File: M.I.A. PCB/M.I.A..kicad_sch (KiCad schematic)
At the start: 41 parts, among them J1 USB_C_Receptacle_USB2.0_16P, SW1 SW_Push, SW2 SW_Push, U1 W25Q128JVS, U2 RP2350B-QFN80, Y1 ABM8-272-T3

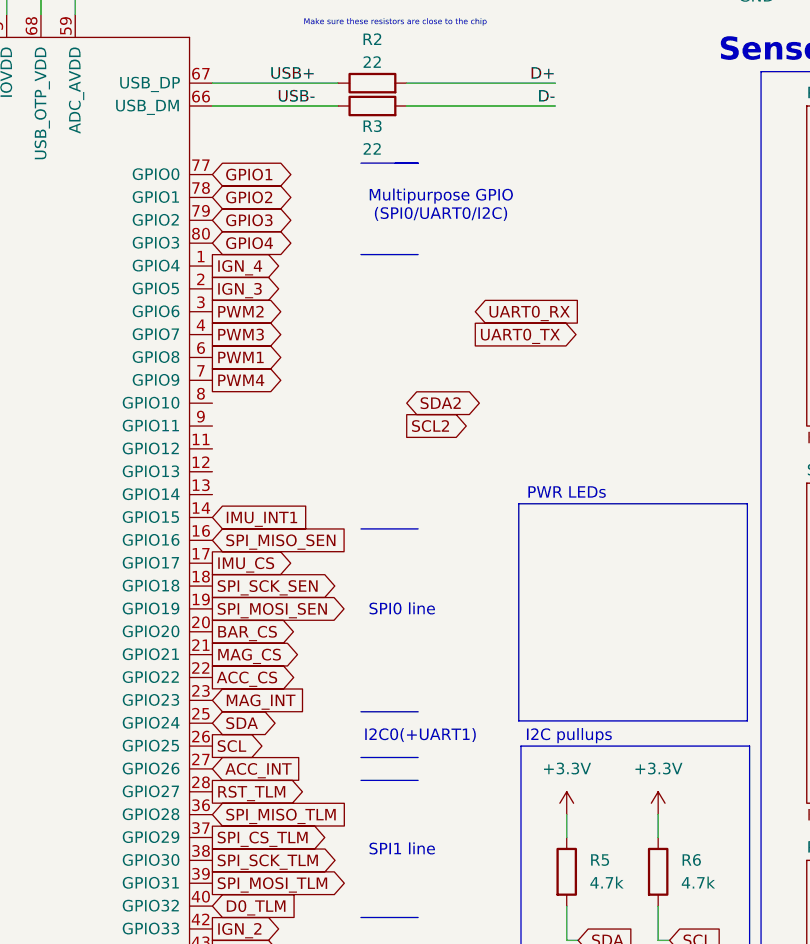
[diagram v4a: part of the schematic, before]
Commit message: Routed GPS Maybe Correctly
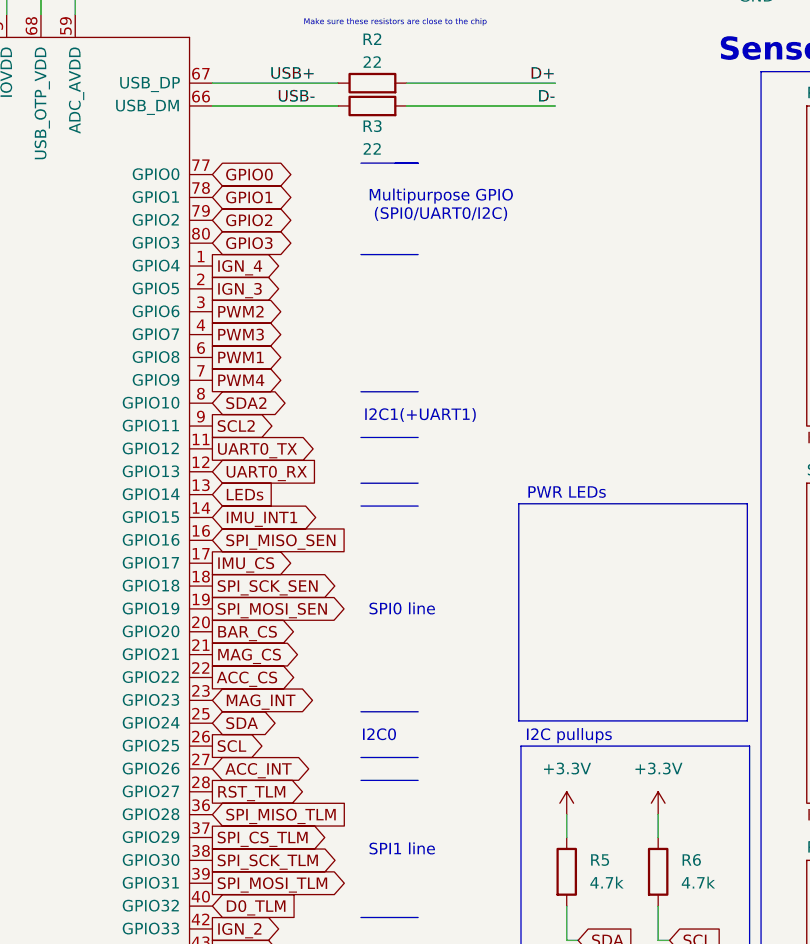
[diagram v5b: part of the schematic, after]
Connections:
- net GPIO4 is gone; now on net GPIO3: U2.80 (GPIO3)
- net GPIO1: now also U2.78 (GPIO1); no longer U2.77 (GPIO0)
- net GPIO2: now also U2.79 (GPIO2); no longer U2.78 (GPIO1)
- net GPIO3: no longer U2.79 (GPIO2)
- net SCL2: now also U2.9 (GPIO11)
- net SDA2: now also U2.8 (GPIO10)
- net UART0_RX: now also U2.12 (GPIO13)
- net UART0_TX: now also U2.11 (GPIO12)
- net LEDs: now reaches U2.13 (GPIO14)
- new net GPIO0: U2.77 (GPIO0)
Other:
- note added: "I2C0"
- note added: "I2C1(+UART1)"
- note removed: "I2C0(+UART1)"
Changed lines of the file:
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@@
 		)
 	)
-	(text "I2C0(+UART1)"
+	(text "I2C0"
 		(exclude_from_sim no)
-		(at 189.484 112.014 0)
+		(at 184.912 112.014 0)
+		(effects
+			(font
+				(size 1.27 1.27)
+			)
+		)
+	)
+	(text "I2C1(+UART1)"
+		(exclude_from_sim no)
+		(at 189.484 76.454 0)
 		(effects
 			(font
@@
 		)
 	)
+	(polyline
+		(pts
+			(xy 182.88 83.82) (xy 189.23 83.82)
+		)
+		(stroke
+			(width 0)
+			(type default)
+		)
+	)
 	(wire
 		(pts
@@
 		)
 	)
+	(polyline
+		(pts
+			(xy 182.88 78.74) (xy 189.23 78.74)
+		)
+		(stroke
+			(width 0)
+			(type default)
+		)
+	)
 	(wire
 		(pts
@@
 	(polyline
 		(pts
-			(xy 182.88 88.9) (xy 189.23 88.9)
+			(xy 182.88 86.36) (xy 189.23 86.36)
 		)
 		(stroke
@@
 		)
 	)
+	(polyline
+		(pts
+			(xy 182.88 73.66) (xy 189.23 73.66)
+		)
+		(stroke
+			(width 0)
+			(type default)
+		)
+	)
 	(wire
 		(pts
@@
 	)
 	(global_label "MAG_INT"
-		(shape input)
+		(shape bidirectional)
 		(at 166.37 107.95 0)
 		(fields_autoplaced yes)
@@
 		)
 		(property "Intersheetrefs" "${INTERSHEET_REFS}"
-			(at 176.8543 107.95 0)
+			(at 178.147 107.95 0)
 			(effects
 				(font
@@
 	(global_label "UART0_TX"
 		(shape output)
-		(at 195.58 67.31 0)
+		(at 166.37 80.01 0)
 		(fields_autoplaced yes)
 		(effects
@@
 		)
 		(property "Intersheetrefs" "${INTERSHEET_REFS}"
-			(at 207.5761 67.31 0)
+			(at 178.3661 80.01 0)
 			(effects
 				(font
@@
 		)
 	)
+	(global_label "GPIO0"
+		(shape bidirectional)
+		(at 166.37 49.53 0)
+		(fields_autoplaced yes)
+		(effects
+			(font
+				(size 1.27 1.27)
+			)
+			(justify left)
+		)
+		(property "Intersheetrefs" "${INTERSHEET_REFS}"
+			(at 176.1513 49.53 0)
+			(effects
+				(font
+					(size 1.27 1.27)
+				)
+				(justify left)
+				(hide yes)
+			)
+		)
+	)
 	(global_label "PWM4"
 		(shape output)
@@
 	(global_label "GPIO1"
 		(shape bidirectional)
-		(at 166.37 49.53 0)
+		(at 166.37 52.07 0)
 		(fields_autoplaced yes)
 		(effects
@@
 		)
 		(property "Intersheetrefs" "${INTERSHEET_REFS}"
-			(at 176.1513 49.53 0)
+			(at 176.1513 52.07 0)
 			(effects
 				(font
@@
 	(global_label "UART0_RX"
 		(shape input)
-		(at 195.58 64.77 0)
+		(at 166.37 82.55 0)
 		(fields_autoplaced yes)
 		(effects
@@
 		)
 		(property "Intersheetrefs" "${INTERSHEET_REFS}"
-			(at 207.8785 64.77 0)
+			(at 178.6685 82.55 0)
 			(effects
 				(font
@@
 	(global_label "GPIO3"
 		(shape bidirectional)
-		(at 166.37 54.61 0)
+		(at 166.37 57.15 0)
 		(fields_autoplaced yes)
 		(effects
@@
 		)
 		(property "Intersheetrefs" "${INTERSHEET_REFS}"
-			(at 176.1513 54.61 0)
+			(at 176.1513 57.15 0)
 			(effects
 				(font
@@
 	(global_label "SDA2"
 		(shape bidirectional)
-		(at 187.96 74.93 0)
+		(at 166.37 74.93 0)
 		(fields_autoplaced yes)
 		(effects
@@
 		)
 		(property "Intersheetrefs" "${INTERSHEET_REFS}"
-			(at 196.8341 74.93 0)
+			(at 175.2441 74.93 0)
 			(effects
 				(font
@@
 	)
 	(global_label "IMU_INT1"
-		(shape input)
+		(shape bidirectional)
 		(at 166.37 87.63 0)
 		(fields_autoplaced yes)
@@
 		)
 		(property "Intersheetrefs" "${INTERSHEET_REFS}"
-			(at 177.8219 87.63 0)
+			(at 178.9332 87.63 0)
 			(effects
 				(font
@@
 		)
 	)
+	(global_label "LEDs"
+		(shape input)
+		(at 166.37 85.09 0)
+		(fields_autoplaced yes)
+		(effects
+			(font
+				(size 1.27 1.27)
+			)
+			(justify left)
+		)
+		(property "Intersheetrefs" "${INTERSHEET_REFS}"
+			(at 173.8304 85.09 0)
+			(effects
+				(font
+					(size 1.27 1.27)
+				)
+				(justify left)
+				(hide yes)
+			)
+		)
+	)
 	(global_label "Cont_Sense2"
 		(shape output)
@@
 	(global_label "GPIO2"
 		(shape bidirectional)
-		(at 166.37 52.07 0)
+		(at 166.37 54.61 0)
 		(fields_autoplaced yes)
 		(effects
@@
 		)
 		(property "Intersheetrefs" "${INTERSHEET_REFS}"
-			(at 176.1513 52.07 0)
+			(at 176.1513 54.61 0)
 			(effects
 				(font
@@
 		)
 	)
-	(global_label "GPIO4"
-		(shape bidirectional)
-		(at 166.37 57.15 0)
-		(fields_autoplaced yes)
-		(effects
-			(font
-				(size 1.27 1.27)
-			)
-			(justify left)
-		)
-		(property "Intersheetrefs" "${INTERSHEET_REFS}"
-			(at 176.1513 57.15 0)
-			(effects
-				(font
-					(size 1.27 1.27)
-				)
-				(justify left)
-				(hide yes)
-			)
-		)
-	)
 	(global_label "SPI_SCK_SD"
 		(shape output)
@@
 	)
 	(global_label "ACC_INT"
-		(shape input)
+		(shape bidirectional)
 		(at 166.37 115.57 0)
 		(fields_autoplaced yes)
@@
 		)
 		(property "Intersheetrefs" "${INTERSHEET_REFS}"
-			(at 177.0357 115.57 0)
+			(at 177.9656 115.57 0)
 			(effects
 				(font
@@
 	(global_label "SCL2"
 		(shape output)
-		(at 187.96 77.47 0)
+		(at 166.37 77.47 0)
 		(fields_autoplaced yes)
 		(effects
@@
 		)
 		(property "Intersheetrefs" "${INTERSHEET_REFS}"
-			(at 195.6623 77.47 0)
+			(at 174.0723 77.47 0)
 			(effects
 				(font

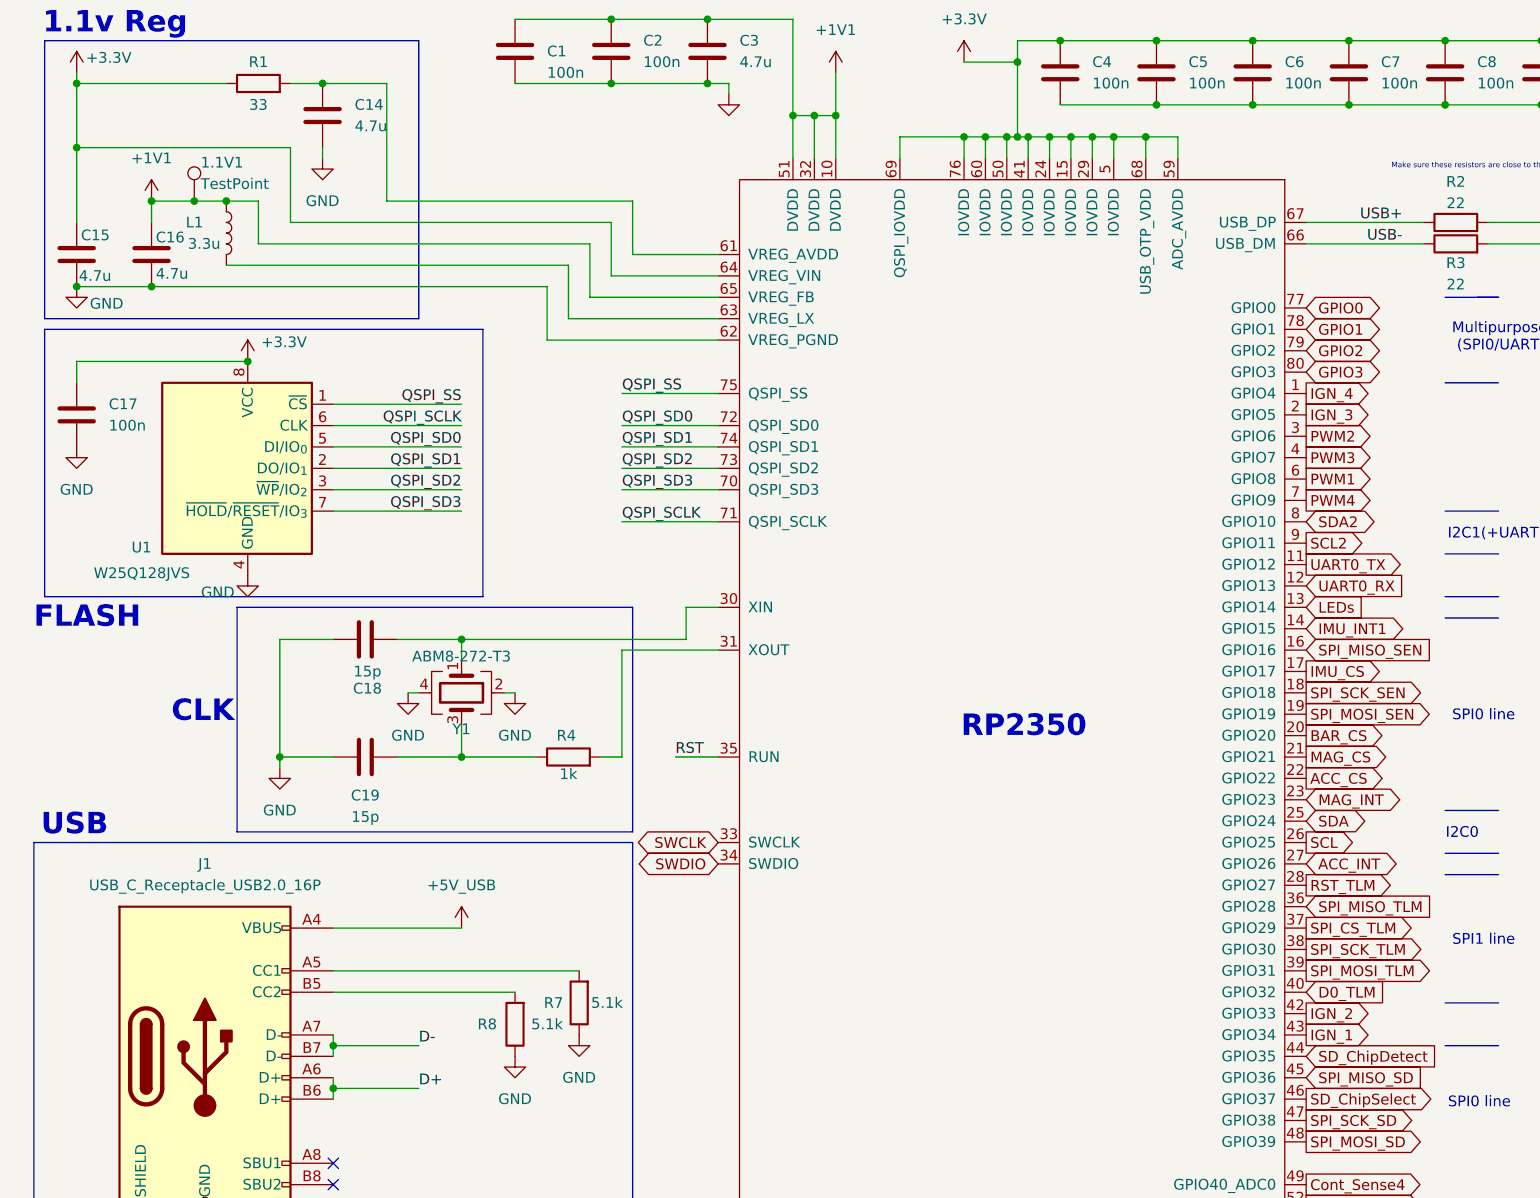
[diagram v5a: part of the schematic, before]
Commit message: Routed two ignition lines
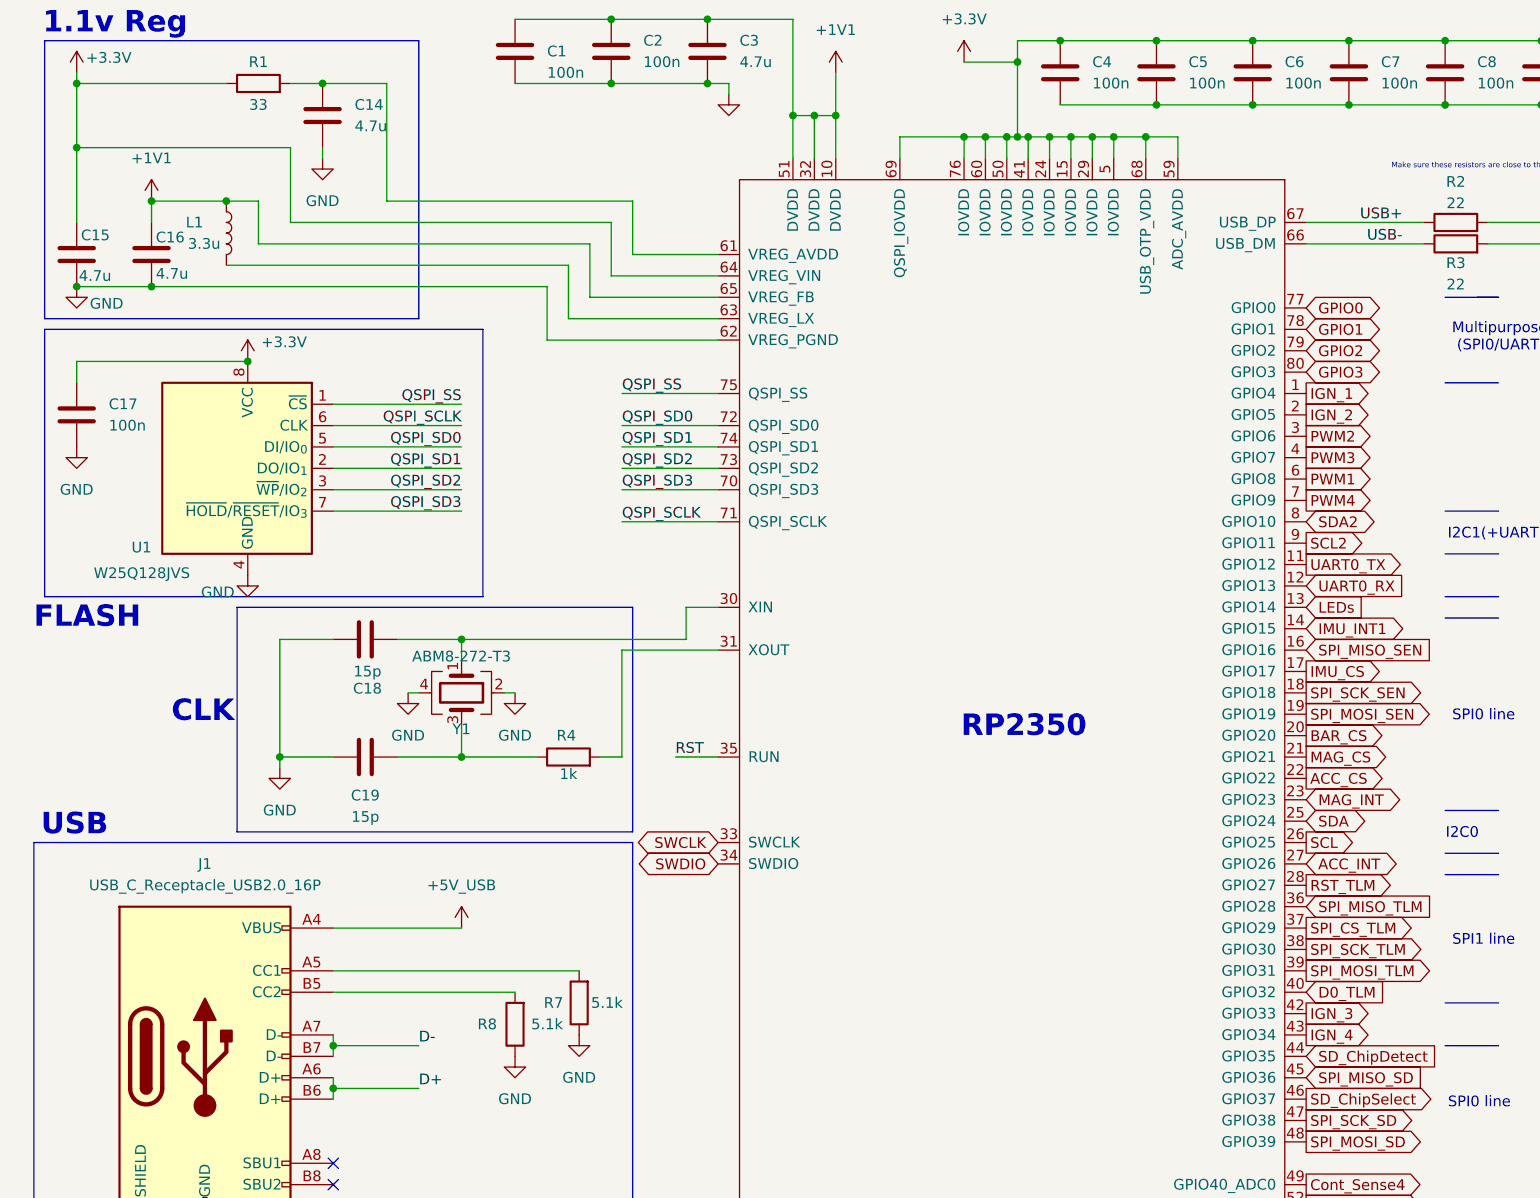
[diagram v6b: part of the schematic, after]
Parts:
- removed 1.1V1: TestPoint, TestPoint:TestPoint_Pad_D1.0mm, symbol Connector:TestPoint
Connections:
- net IGN_1: now also U2.1 (GPIO4); no longer U2.43 (GPIO34)
- net IGN_2: now also U2.2 (GPIO5); no longer U2.42 (GPIO33)
- net IGN_3: now also U2.42 (GPIO33); no longer U2.2 (GPIO5)
- net IGN_4: now also U2.43 (GPIO34); no longer U2.1 (GPIO4)
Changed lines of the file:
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@@
 	)
 	(junction
-		(at 34.29 36.83)
-		(diameter 0)
-		(color 0 0 0 0)
-	)
-	(junction
 		(at 83.82 22.86)
 		(diameter 0)
@@
 	(wire
 		(pts
-			(xy 34.29 36.83) (xy 29.21 36.83)
+			(xy 29.21 36.83) (xy 38.1 36.83)
 		)
 		(stroke
@@
 	(wire
 		(pts
-			(xy 38.1 36.83) (xy 34.29 36.83)
-		)
-		(stroke
-			(width 0)
-			(type default)
-		)
-	)
-	(wire
-		(pts
 			(xy 60.96 181.61) (xy 63.5 181.61)
 		)
@@
 	(global_label "IGN_3"
 		(shape output)
-		(at 166.37 62.23 0)
+		(at 166.37 133.35 0)
 		(fields_autoplaced yes)
 		(effects
@@
 		)
 		(property "Intersheetrefs" "${INTERSHEET_REFS}"
-			(at 174.7376 62.23 0)
+			(at 174.7376 133.35 0)
 			(effects
 				(font
@@
 	(global_label "IGN_2"
 		(shape output)
-		(at 166.37 133.35 0)
+		(at 166.37 62.23 0)
 		(fields_autoplaced yes)
 		(effects
@@
 		)
 		(property "Intersheetrefs" "${INTERSHEET_REFS}"
-			(at 174.7376 133.35 0)
+			(at 174.7376 62.23 0)
 			(effects
 				(font
@@
 	(global_label "IGN_1"
 		(shape output)
-		(at 166.37 135.89 0)
+		(at 166.37 59.69 0)
 		(fields_autoplaced yes)
 		(effects
@@
 		)
 		(property "Intersheetrefs" "${INTERSHEET_REFS}"
-			(at 174.7376 135.89 0)
+			(at 174.7376 59.69 0)
 			(effects
 				(font
@@
 	(global_label "IGN_4"
 		(shape output)
-		(at 166.37 59.69 0)
+		(at 166.37 135.89 0)
 		(fields_autoplaced yes)
 		(effects
@@
 		)
 		(property "Intersheetrefs" "${INTERSHEET_REFS}"
-			(at 174.7376 59.69 0)
+			(at 174.7376 135.89 0)
 			(effects
 				(font
@@
 					(unit 1)
 				)
-			)
-		)
-	)
-	(symbol
-		(lib_id "Connector:TestPoint")
-		(at 34.29 36.83 0)
-		(unit 1)
-		(exclude_from_sim no)
-		(in_bom yes)
-		(on_board yes)
-		(dnp no)
-		(property "Reference" "1.1V1"
-			(at 35.052 32.258 0)
-			(effects
-				(font
-					(size 1.27 1.27)
-				)
-				(justify left)
-			)
-		)
-		(property "Value" "TestPoint"
-			(at 35.052 34.798 0)
-			(effects
-				(font
-					(size 1.27 1.27)
-				)
-				(justify left)
-			)
-		)
-		(property "Footprint" "TestPoint:TestPoint_Pad_D1.0mm"
-			(at 39.37 36.83 0)
-			(effects
-				(font
-					(size 1.27 1.27)
-				)
-				(hide yes)
-			)
-		)
-		(property "Datasheet" "~"
-			(at 39.37 36.83 0)
-			(effects
-				(font
-					(size 1.27 1.27)
-				)
-				(hide yes)
-			)
-		)
-		(property "Description" "test point"
-			(at 34.29 36.83 0)
-			(effects
-				(font
-					(size 1.27 1.27)
-				)
-				(hide yes)
-			)
-		)
-		(property "LCSC" ""
-			(at 34.29 36.83 0)
-			(effects
-				(font
-					(size 1.27 1.27)
-				)
-				(hide yes)
-			)
-		)
-		(property "Manufacturer" ""
-			(at 34.29 36.83 0)
-			(effects
-				(font
-					(size 1.27 1.27)
-				)
-				(hide yes)
-			)
-		)
-		(property "Manufacturer Part" ""
-			(at 34.29 36.83 0)
-			(effects
-				(font
-					(size 1.27 1.27)
-				)
-				(hide yes)
-			)
-		)
-		(pin "1"
-		)
-		(instances
-			(project "M.I.A."
-				(path "/4d55825e-4251-44bf-9376-9abd9228f348"
-					(reference "1.1V1")
-					(unit 1)
-				)

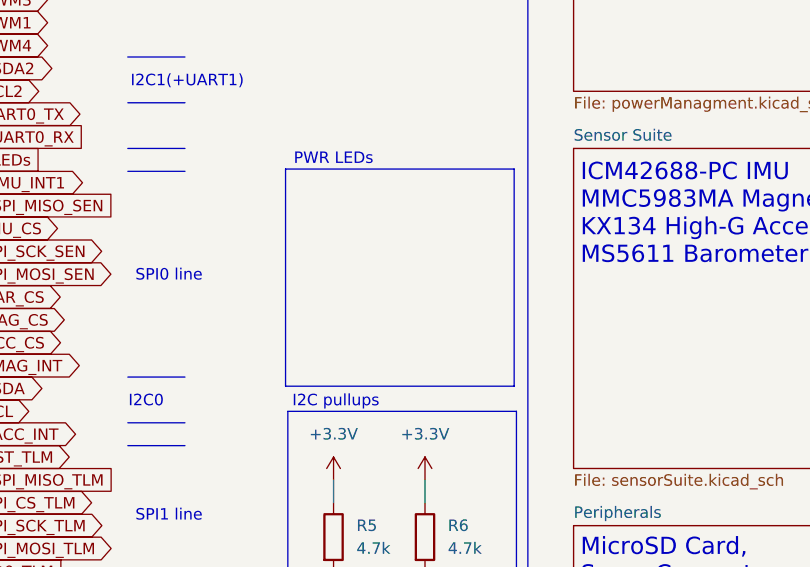
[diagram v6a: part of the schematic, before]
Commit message: Added LEDs, Prepped for 4 layer conversion
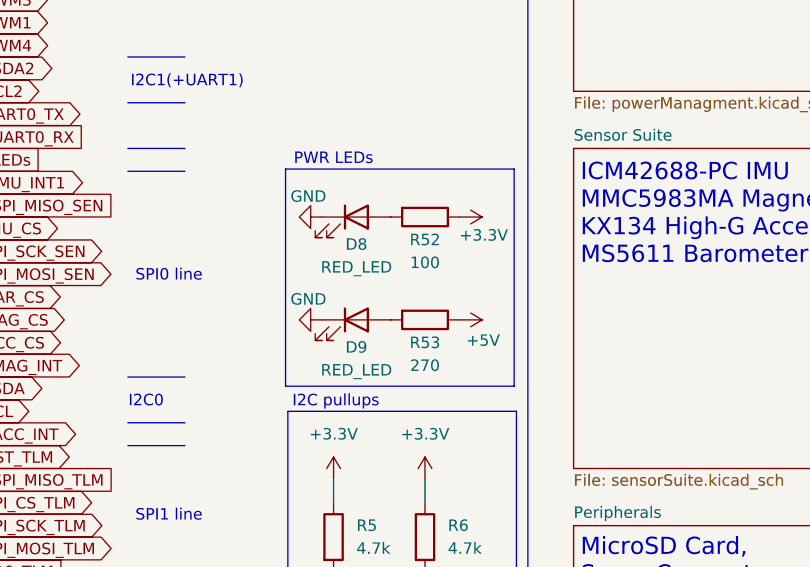
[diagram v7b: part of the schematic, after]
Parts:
- added D8, D9: RED_LED, LED_SMD:LED_0805_2012Metric, symbol Device:LED
- added R52: 100, Resistor_SMD:R_0603_1608Metric, symbol Device:R
- added R53: 270, Resistor_SMD:R_0603_1608Metric, symbol Device:R
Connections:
- net +3.3V: now also R52.1
- net GND: now also D8.1 (K), D9.1 (K)
- new net: D8.2 (A), R52.2
- new net: D9.2 (A), R53.2
- new net +5V: R53.1
